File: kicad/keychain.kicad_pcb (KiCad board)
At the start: 2 copper layers, 68 x 64 mm, 53 parts, among them J1 OLED 1.5in SSD1327, J2 LiPo 3.7V, J3 USB-C, SW1 USER1, SW2 USER2, SW3 PWR, SW4 BOOT, SW5 RST, U1 ESP32-C6-MINI-1, U2 MCP73831, U3 AP2112K-3.3, U4 TLV61046A, U5 74AHCT1G125, U6 ESDA6V1-5SC6

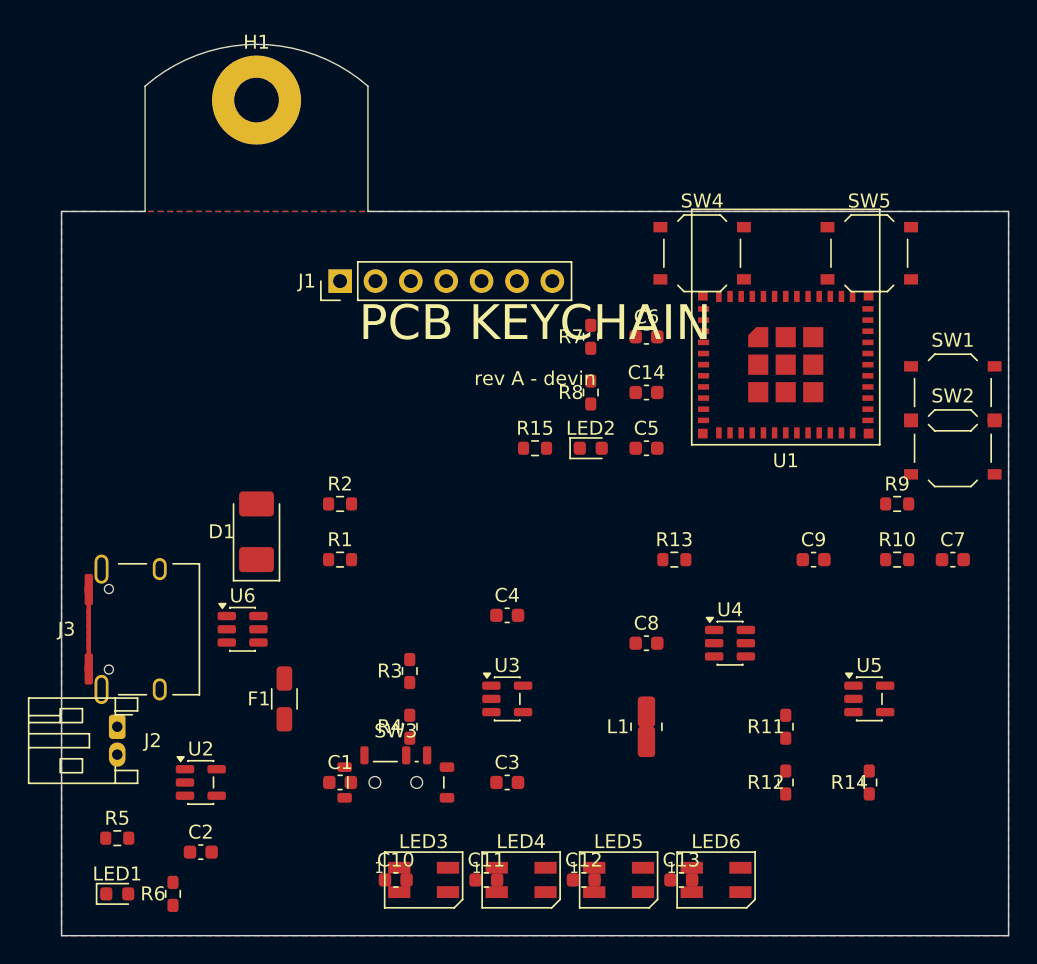
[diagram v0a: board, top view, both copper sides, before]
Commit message: Rework PCB: fix pad rotation, new placement, grid router
- generator: pads now store board-frame rotation (footprint rot +
  pad rot); hidden silk text; U1 courtyard shrunk to module body and
  antenna rule-area moved to an explicit keepout zone
- placement rewritten around real courtyard extents; USB-C left,
  JST top-left, OLED header top, RGB chain + buttons bottom
- tools/router.py: deterministic bounded A* two-layer router
- tools/check_layout.py: courtyard-overlap sanity checker

Generated with [Devin](https://devin.ai)

Co-Authored-By: Devin <158243242+devin-ai-integration[bot]@users.noreply.github.com>
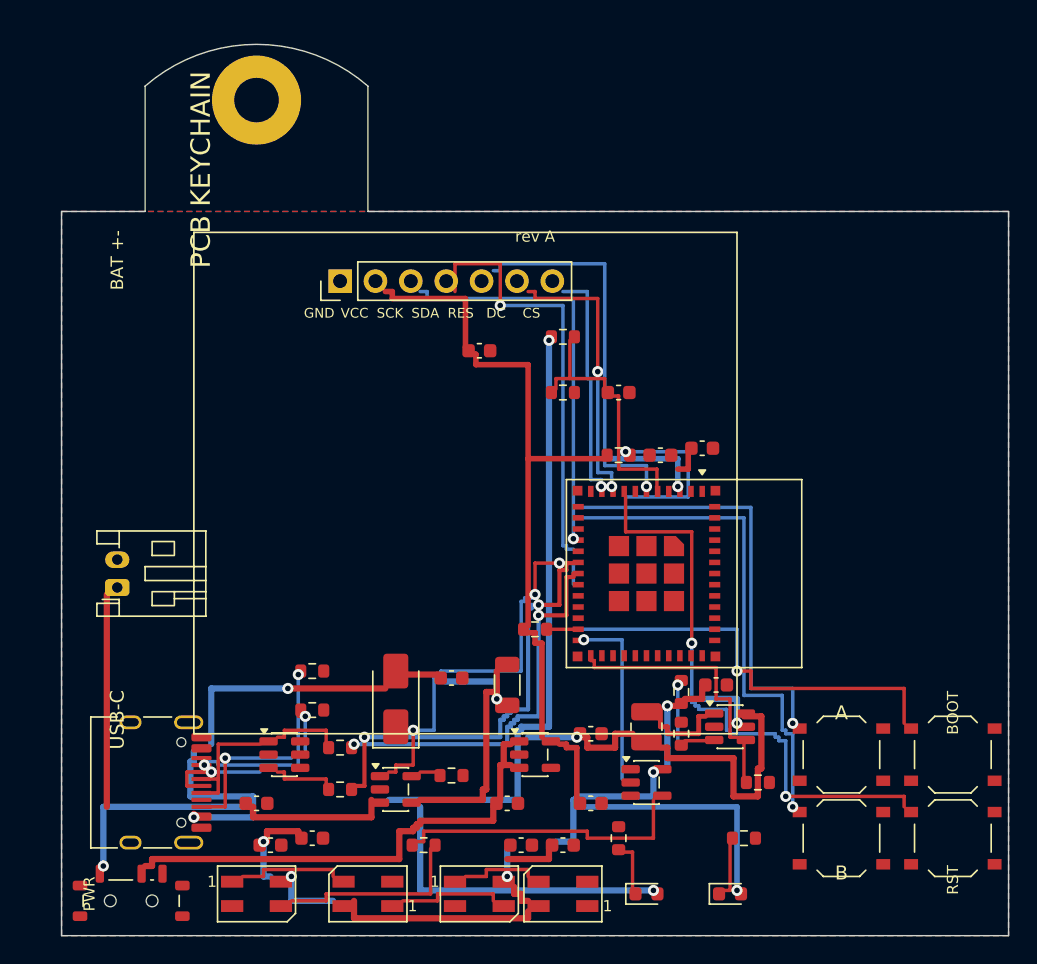
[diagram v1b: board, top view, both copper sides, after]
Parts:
- moved SW5 42.4 mm to (84.0, 70.0)
- moved SW4 40.2 mm to (84.0, 64.0)
- moved LED1 38.0 mm to (62.0, 74.0)
- moved LED2 33.5 mm to (68.0, 74.0)
- moved R14 32.3 mm to (46.0, 70.5), turned to 0 degrees
- moved R6 32.2 mm to (60.0, 70.0)
- moved R15 31.8 mm to (69.0, 70.0)
- moved SW2 29.1 mm to (76.0, 70.0)
- moved SW1 27.2 mm to (76.0, 64.0)
- moved C7 26.8 mm to (60.0, 38.0)
- moved R10 26.8 mm to (56.0, 38.0)
- moved R9 26.8 mm to (56.0, 34.0)
- moved R5 24.4 mm to (48.0, 65.5)
- moved SW3 20.8 mm to (25.0, 74.5)
- moved U1 18.0 mm to (62.0, 51.0), turned to 270 degrees
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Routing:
- net VBAT: track 0.00 -> 84.8 mm, vias 0 -> 2
- net +3V3: track 0.00 -> 78.2 mm, vias 0 -> 2
- net VBAT_SYS: track 0.00 -> 61.0 mm, vias 0 -> 1
- net +5V: track 0.00 -> 57.0 mm, vias 0 -> 6
- net EN: track 0.00 -> 55.0 mm, vias 0 -> 3
- net VBUS: track 0.00 -> 37.8 mm, vias 0 -> 3
- net VBUS_F: track 0.00 -> 37.5 mm, vias 0 -> 1
- net USER2: track 0.00 -> 35.8 mm, vias 0 -> 1
- net USB_DM: track 0.00 -> 31.8 mm, vias 0 -> 2
- net BOOT: track 0.00 -> 31.5 mm, vias 0 -> 1
- net OLED_MOSI: track 0.00 -> 31.0 mm, vias 0 -> 1
- net USER1: track 0.00 -> 30.5 mm, vias 0 -> 1
- net CHG_STAT: track 0.00 -> 29.8 mm, vias 0 -> 3
- net OLED_SCK: track 0.00 -> 28.8 mm, vias 0 -> 1
- net USB_DP: track 0.00 -> 28.0 mm, vias 0 -> 2
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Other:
- board text added: "A"
- board text added: "B"
- board text added: "BAT +-"
- board text added: "BOOT"
- board text added: "CS"
- board text added: "DC"
- board text added: "GND"
- board text added: "PWR"
- board text added: "RES"
- board text added: "RST"
- board text added: "SCK"
- board text added: "SDA"
- board text added: "USB-C"
- board text added: "VCC"
- board text added: "rev A"
- board text removed: "rev A - devin"
